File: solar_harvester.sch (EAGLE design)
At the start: 44 parts, among them U1 BQ25505, U2 TPS61322XA, U3 TPS61322XA, U4 MAX17040, U5 INA226, U6 DMP3085LSD

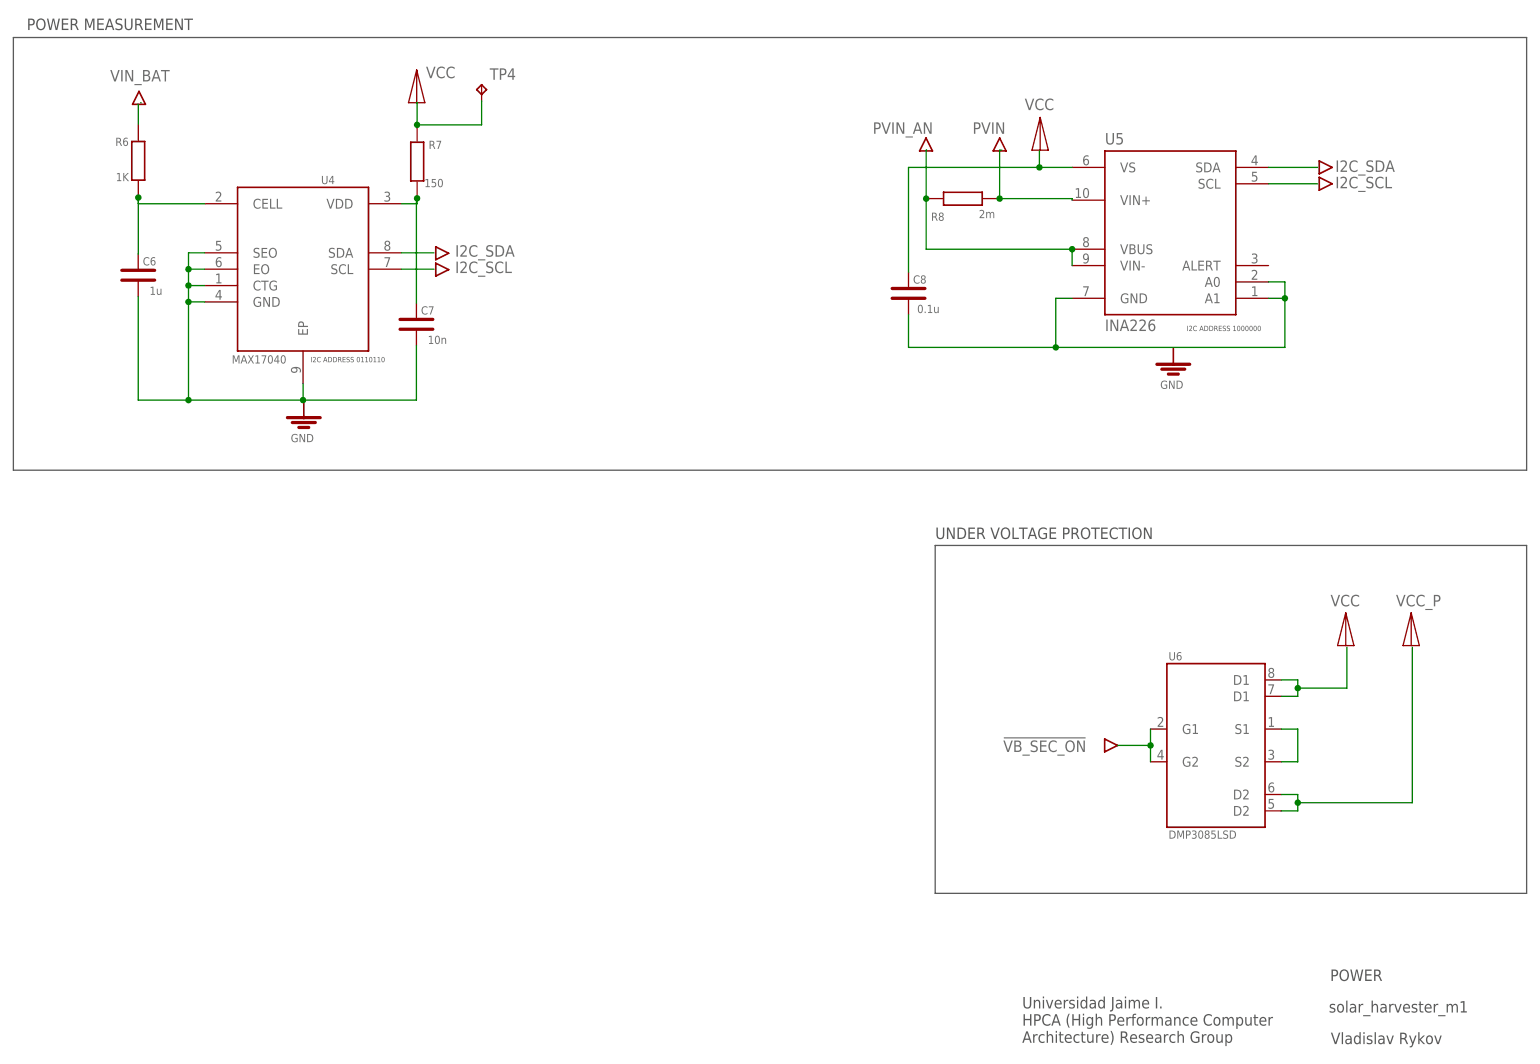
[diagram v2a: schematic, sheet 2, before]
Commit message: alt measurement ics vin added, drc & gnd rev done
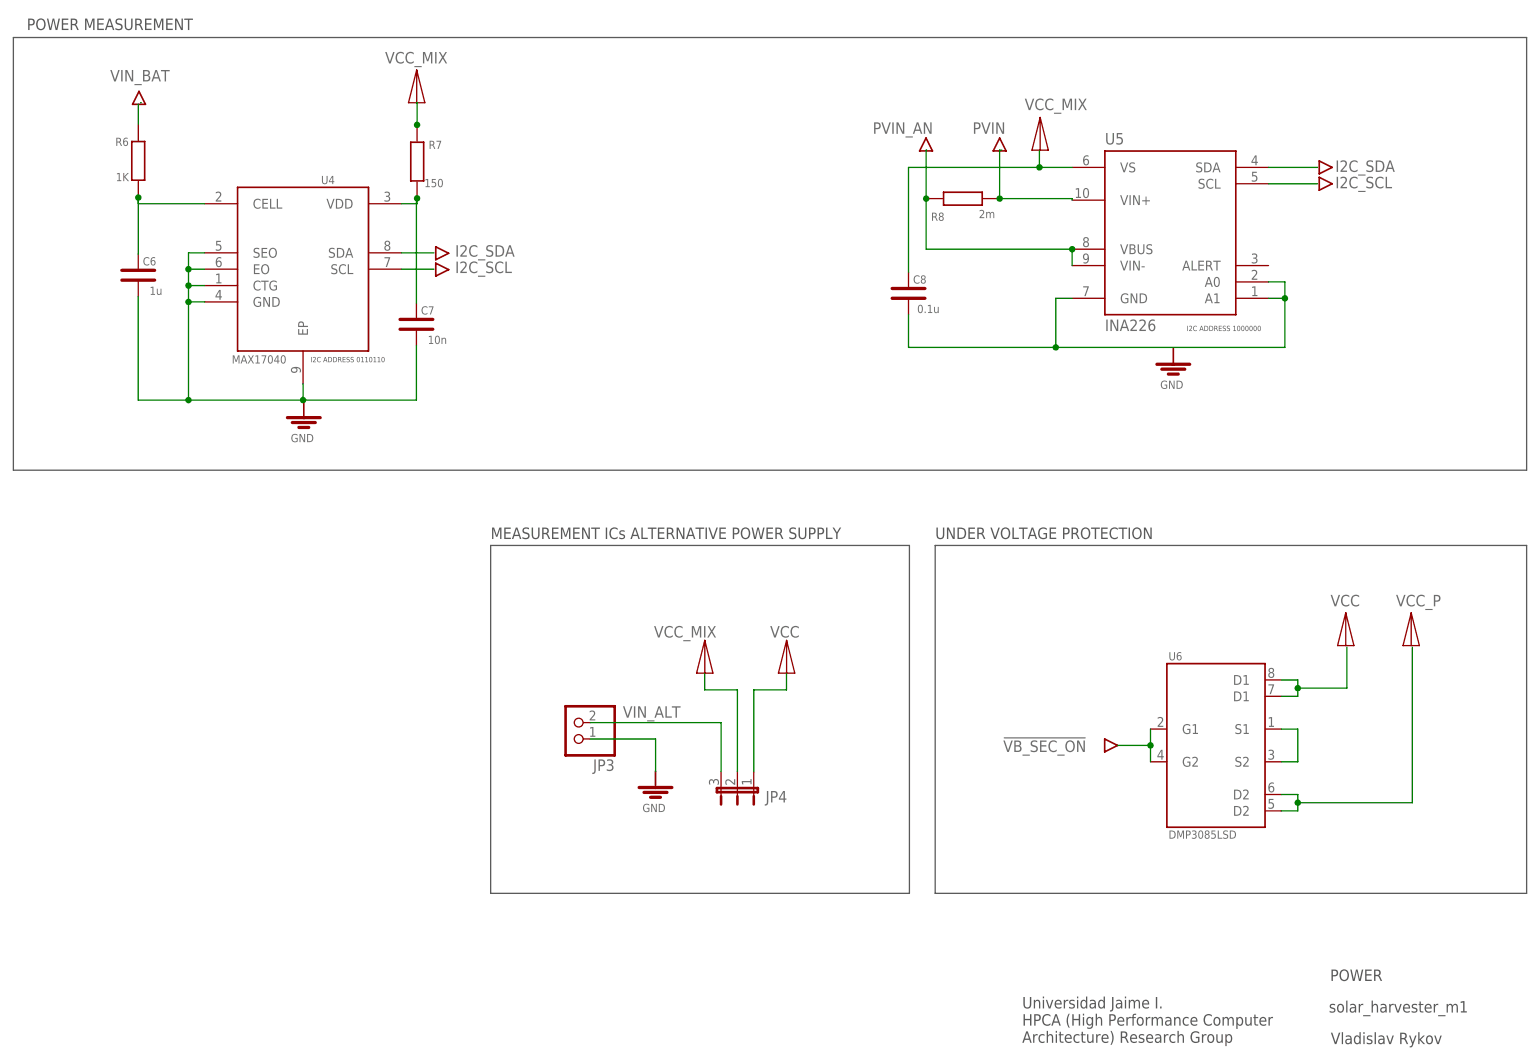
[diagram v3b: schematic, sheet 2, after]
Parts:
- removed U$36: FIDUCIAL_50, vrlib_prod:FIDUCIAL_50
- added FID2: FIDUCIAL_25, vrlib_prod:FIDUCIAL_25
- added JP3: (no value), pinhead:PINHD-1X2
- added JP4: (no value), vrlib_jumper:JP2E
- B1: value SOLAR_HARVESTER_M1_BOARD -> SOLAR_HARVESTER_V1.0_M1_BOARD; device vrlib_board:SOLAR_HARVESTER_M1_BOARD -> vrlib_board:SOLAR_HARVESTER_V1.0_M1_BOARD
- FID1: value FIDUCIAL_50 -> FIDUCIAL_25; device vrlib_prod:FIDUCIAL_50 -> vrlib_prod:FIDUCIAL_25
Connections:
- new net VCC_MIX: C8.1, JP4.2, R7.P$2, U5.VS
- new net VIN_ALT: JP3.2, JP4.3
- net GND: now also JP3.1
- net VCC: now also JP4.1; no longer C8.1, R7.P$2, U5.VS
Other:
- note added: "MEASUREMENT ICs ALTERNATIVE POWER SUPPLY"
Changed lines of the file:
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@@
 <part name="C9" library="vrlib_caps" deviceset="1608_CAP" device="" value="22u"/>
 <part name="C10" library="vrlib_caps" deviceset="1608_CAP" device="" value="22u"/>
-<part name="B1" library="vrlib_board" deviceset="SOLAR_HARVESTER_M1_BOARD" device=""/>
+<part name="B1" library="vrlib_board" deviceset="SOLAR_HARVESTER_V1.0_M1_BOARD" device=""/>
 <part name="JP1" library="pinhead" library_urn="urn:adsk.eagle:library:325" deviceset="PINHD-1X3" device="" package3d_urn="urn:adsk.eagle:package:22458/2"/>
 <part name="U$7" library="vrlib_com_symbols" deviceset="LOUT" device=""/>
@@
 <part name="TP2" library="testpad" library_urn="urn:adsk.eagle:library:385" deviceset="TP" device="TP10SQ" package3d_urn="urn:adsk.eagle:package:27962/1"/>
 <part name="TP3" library="testpad" library_urn="urn:adsk.eagle:library:385" deviceset="TP" device="TP10SQ" package3d_urn="urn:adsk.eagle:package:27962/1"/>
-<part name="TP4" library="testpad" library_urn="urn:adsk.eagle:library:385" deviceset="TP" device="TP10SQ" package3d_urn="urn:adsk.eagle:package:27962/1"/>
 <part name="TP5" library="testpad" library_urn="urn:adsk.eagle:library:385" deviceset="TP" device="TP10SQ" package3d_urn="urn:adsk.eagle:package:27962/1"/>
 <part name="TP6" library="testpad" library_urn="urn:adsk.eagle:library:385" deviceset="TP" device="TP10SQ" package3d_urn="urn:adsk.eagle:package:27962/1"/>
-<part name="FID1" library="vrlib_prod" deviceset="FIDUCIAL_50" device=""/>
-<part name="U$36" library="vrlib_prod" deviceset="FIDUCIAL_50" device=""/>
+<part name="FID1" library="vrlib_prod" deviceset="FIDUCIAL_25" device=""/>
+<part name="FID2" library="vrlib_prod" deviceset="FIDUCIAL_25" device=""/>
+<part name="JP3" library="pinhead" library_urn="urn:adsk.eagle:library:325" deviceset="PINHD-1X2" device="" package3d_urn="urn:adsk.eagle:package:22435/2"/>
+<part name="JP4" library="vrlib_jumper" deviceset="JP2E" device="" package3d_urn="urn:adsk.eagle:package:15452/1"/>
+<part name="U$35" library="vrlib_com_symbols" deviceset="VCC" device=""/>
+<part name="U$36" library="vrlib_com_symbols" deviceset="VCC" device=""/>
+<part name="U$37" library="vrlib_com_symbols" deviceset="GND" device=""/>
+<part name="TP4" library="testpad" library_urn="urn:adsk.eagle:library:385" deviceset="TP" device="TP10SQ" package3d_urn="urn:adsk.eagle:package:27962/1"/>
 </parts>
 <sheets>
@@
 <attribute name="NAME" x="68.072" y="18.288" size="1.27" layer="95"/>
 </instance>
-<instance part="U$36" gate="G$1" x="83.82" y="12.7" smashed="yes">
+<instance part="FID2" gate="G$1" x="83.82" y="12.7" smashed="yes">
 <attribute name="NAME" x="80.772" y="18.288" size="1.27" layer="95"/>
+</instance>
+<instance part="TP4" gate="G$1" x="194.188" y="142.152" smashed="yes" rot="R270">
+<attribute name="NAME" x="191.604" y="138.816" size="1.778" layer="95"/>
+<attribute name="TP_SIGNAL_NAME" x="192.918" y="140.882" size="1.778" layer="97" rot="R270"/>
 </instance>
 </instances>
@@
 <wire x1="187.38" y1="101.6" x2="187.96" y2="101.6" width="0.1524" layer="91"/>
 <wire x1="187.38" y1="150.2" x2="187.38" y2="157.48" width="0.1524" layer="91"/>
-<junction x="187.38" y="150.2"/>
+<junction x="187.38" y="142.072"/>
 <label x="184.712" y="163.02" size="1.778" layer="95"/>
+<pinref part="TP4" gate="G$1" pin="TP"/>
+<wire x1="187.38" y1="150.2" x2="187.38" y2="142.108" width="0.1524" layer="91"/>
+<wire x1="187.38" y1="142.108" x2="191.648" y2="142.152" width="0.1524" layer="91"/>
 </segment>
 </net>
@@
 <wire x1="156" y1="88" x2="247.8" y2="88" width="0.1524" layer="97"/>
 <text x="156" y="89" size="1.778" layer="97">UNDER VOLTAGE PROTECTION</text>
+<wire x1="152" y1="88" x2="152" y2="34" width="0.1524" layer="97"/>
+<wire x1="152" y1="34" x2="87" y2="34" width="0.1524" layer="97"/>
+<wire x1="87" y1="34" x2="87" y2="88" width="0.1524" layer="97"/>
+<wire x1="87" y1="88" x2="152" y2="88" width="0.1524" layer="97"/>
+<text x="87" y="89" size="1.778" layer="97">MEASUREMENT ICs ALTERNATIVE POWER SUPPLY</text>
 </plain>
 <instances>
@@
 <instance part="U$33" gate="G$1" x="219.726" y="72.454" smashed="yes"/>
 <instance part="U$34" gate="G$1" x="229.886" y="72.454" smashed="yes"/>
-<instance part="TP4" gate="G$1" x="85.598" y="159.512" smashed="yes">
-<attribute name="NAME" x="86.868" y="160.274" size="1.778" layer="95"/>
-<attribute name="TP_SIGNAL_NAME" x="86.868" y="158.242" size="1.778" layer="97"/>
-</instance>
+<instance part="JP3" gate="G$1" x="99.9" y="60.5" smashed="yes" rot="R180">
+<attribute name="NAME" x="106.25" y="54.785" size="1.778" layer="95" rot="R180"/>
+<attribute name="VALUE" x="106.25" y="65.58" size="1.778" layer="96" rot="R180"/>
+</instance>
+<instance part="JP4" gate="1" x="125.3" y="50.34" smashed="yes" rot="R180">
+<attribute name="NAME" x="129.66" y="48.11" size="1.778" layer="95"/>
+<attribute name="VALUE" x="119.585" y="50.34" size="1.778" layer="96" rot="R270"/>
+</instance>
+<instance part="U$35" gate="G$1" x="132.936" y="68.184" smashed="yes"/>
+<instance part="U$36" gate="G$1" x="120.236" y="68.184" smashed="yes"/>
+<instance part="U$37" gate="G$1" x="112.588" y="52.97" smashed="yes"/>
 </instances>
 <busses>
@@
 </segment>
 </net>
-<net name="VIN_BAT" class="0">
-<segment>
-<pinref part="R6" gate="G$1" pin="P$1"/>
-<wire x1="32.316" y1="153.398" x2="32.316" y2="156.464" width="0.1524" layer="91"/>
-<wire x1="32.316" y1="156.464" x2="32.258" y2="156.464" width="0.1524" layer="91"/>
-<label x="27.94" y="160.02" size="1.778" layer="95"/>
-</segment>
-</net>
 <net name="VCC" class="0">
-<segment>
-<pinref part="U5" gate="G$1" pin="VS"/>
-<wire x1="177.26" y1="146.68" x2="172.18" y2="146.68" width="0.1524" layer="91"/>
-<wire x1="172.18" y1="146.68" x2="172.18" y2="149.22" width="0.1524" layer="91"/>
-<label x="169.894" y="155.57" size="1.778" layer="95"/>
-<pinref part="C8" gate="G$1" pin="1"/>
-<wire x1="151.86" y1="130.424" x2="151.86" y2="146.68" width="0.1524" layer="91"/>
-<wire x1="151.86" y1="146.68" x2="172.18" y2="146.68" width="0.1524" layer="91"/>
-<junction x="172.18" y="146.68"/>
-</segment>
-<segment>
-<pinref part="R7" gate="G$1" pin="P$2"/>
-<wire x1="75.584" y1="153.398" x2="75.584" y2="153.282" width="0.1524" layer="91"/>
-<wire x1="75.584" y1="153.282" x2="75.584" y2="156.718" width="0.1524" layer="91"/>
-<wire x1="75.584" y1="156.718" x2="75.438" y2="156.718" width="0.1524" layer="91"/>
-<junction x="75.584" y="153.282"/>
-<label x="76.962" y="160.528" size="1.778" layer="95"/>
-<pinref part="TP4" gate="G$1" pin="TP"/>
-<wire x1="75.584" y1="153.282" x2="85.598" y2="153.282" width="0.1524" layer="91"/>
-<wire x1="85.598" y1="153.282" x2="85.598" y2="156.972" width="0.1524" layer="91"/>
-</segment>
 <segment>
 <pinref part="U6" gate="G$1" pin="D1@1"/>
@@
 <wire x1="212.28" y1="65.85" x2="219.9" y2="65.85" width="0.1524" layer="91"/>
 <wire x1="219.9" y1="65.85" x2="219.9" y2="72.2" width="0.1524" layer="91"/>
+</segment>
+<segment>
+<pinref part="JP4" gate="1" pin="1"/>
+<wire x1="127.84" y1="52.88" x2="127.84" y2="65.58" width="0.1524" layer="91"/>
+<wire x1="127.84" y1="65.58" x2="132.92" y2="65.58" width="0.1524" layer="91"/>
+<wire x1="132.92" y1="65.58" x2="132.92" y2="68.12" width="0.1524" layer="91"/>
+<label x="130.38" y="73.708" size="1.778" layer="95"/>
 </segment>
 </net>
@@
 <junction x="174.72" y="118.74"/>
 </segment>
+<segment>
+<pinref part="JP3" gate="G$1" pin="1"/>
+<wire x1="102.44" y1="57.96" x2="112.6" y2="57.96" width="0.1524" layer="91"/>
+<wire x1="112.6" y1="57.96" x2="112.6" y2="52.88" width="0.1524" layer="91"/>
+</segment>
 </net>
 <net name="N$12" class="0">
@@
 </segment>
 </net>
+<net name="VIN_BAT" class="0">
+<segment>
+<pinref part="R6" gate="G$1" pin="P$1"/>
+<wire x1="32.316" y1="153.398" x2="32.316" y2="156.464" width="0.1524" layer="91"/>
+<wire x1="32.316" y1="156.464" x2="32.258" y2="156.464" width="0.1524" layer="91"/>
+<label x="27.94" y="160.02" size="1.778" layer="95"/>
+</segment>
+</net>
+<net name="VCC_MIX" class="0">
+<segment>
+<wire x1="75.584" y1="156.718" x2="75.438" y2="156.718" width="0.1524" layer="91"/>
+<pinref part="R7" gate="G$1" pin="P$2"/>
+<wire x1="75.584" y1="153.398" x2="75.584" y2="153.282" width="0.1524" layer="91"/>
+<wire x1="75.584" y1="153.282" x2="75.584" y2="156.718" width="0.1524" layer="91"/>
+<junction x="75.584" y="153.282"/>
+<label x="70.612" y="162.814" size="1.778" layer="95"/>
+</segment>
+<segment>
+<pinref part="U5" gate="G$1" pin="VS"/>
+<wire x1="177.26" y1="146.68" x2="172.18" y2="146.68" width="0.1524" layer="91"/>
+<wire x1="172.18" y1="146.68" x2="172.18" y2="149.22" width="0.1524" layer="91"/>
+<label x="169.894" y="155.57" size="1.778" layer="95"/>
+<pinref part="C8" gate="G$1" pin="1"/>
+<wire x1="151.86" y1="130.424" x2="151.86" y2="146.68" width="0.1524" layer="91"/>
+<wire x1="151.86" y1="146.68" x2="172.18" y2="146.68" width="0.1524" layer="91"/>
+<junction x="172.18" y="146.68"/>
+</segment>
+<segment>
+<pinref part="JP4" gate="1" pin="2"/>
+<wire x1="125.3" y1="52.88" x2="125.3" y2="65.58" width="0.1524" layer="91"/>
+<wire x1="125.3" y1="65.58" x2="120.22" y2="65.58" width="0.1524" layer="91"/>
+<wire x1="120.22" y1="65.58" x2="120.22" y2="68.12" width="0.1524" layer="91"/>
+<label x="112.346" y="73.708" size="1.778" layer="95"/>
+</segment>
+</net>
+<net name="VIN_ALT" class="0">
+<segment>
+<pinref part="JP3" gate="G$1" pin="2"/>
+<pinref part="JP4" gate="1" pin="3"/>
+<wire x1="102.44" y1="60.5" x2="122.76" y2="60.5" width="0.1524" layer="91"/>
+<wire x1="122.76" y1="60.5" x2="122.76" y2="52.88" width="0.1524" layer="91"/>
+<label x="107.52" y="61.262" size="1.778" layer="95"/>
+</segment>
+</net>
